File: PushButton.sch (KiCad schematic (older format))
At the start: 0 parts

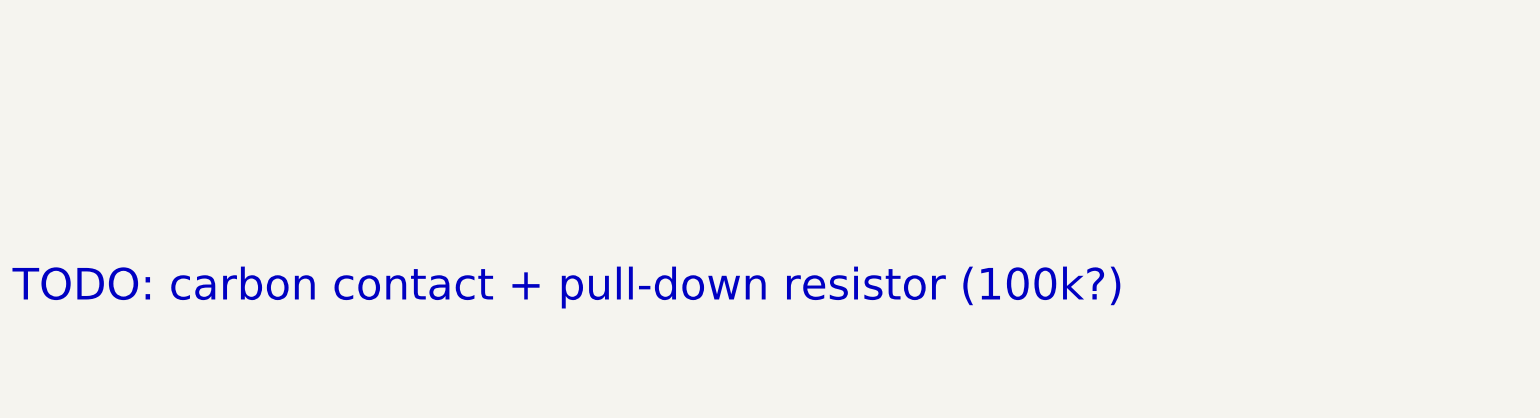
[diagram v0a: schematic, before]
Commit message: Add the push buttons and mounting holes
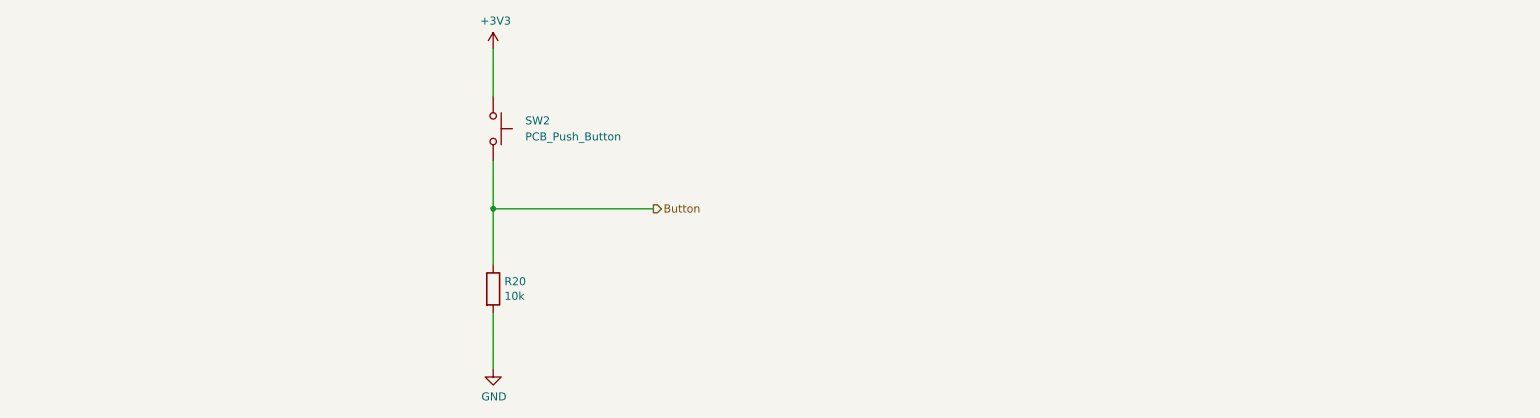
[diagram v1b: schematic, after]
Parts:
- added R19: 10k, Resistor_SMD:R_0603_1608Metric, symbol Device:R
- added SW2: PCB_Push_Button, LitterRobot:PCB_Push_Button_5mm_0.4mm, symbol Switch:SW_Push
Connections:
- new net +3V3: SW2.1
- new net Button: R19.1, SW2.2
- new net GND: R19.2
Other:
- note removed: "TODO: carbon contact + pull-down resistor (100k?)"
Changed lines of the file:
@@
 $Descr A4 11693 8268
 encoding utf-8
-Sheet 10 16
-Title "Litter Robot 3 - Push button"
+Sheet 9 16
+Title "Litter Robot 3 - Push button (single)"
 Date "2021-02-28"
 Rev "A1"
@@
 Comment4 ""
 $EndDescr
-Text Notes 2000 4100 0    197  ~ 0
-TODO: carbon contact + pull-down resistor (100k?)
+$Comp
+L Device:R R?
+U 1 1 604D6269
+P 5000 4000
+AR Path="/603F20AB/604D6269" Ref="R?"  Part="1"
+AR Path="/603F1DCE/604D6269" Ref="R?"  Part="1"
+AR Path="/603E03AA/603C05C6/604D6269" Ref="R?"  Part="1"
+AR Path="/603E03AA/603C0699/604D6269" Ref="R19"  Part="1"
+AR Path="/603E03AA/603C06CF/604D6269" Ref="R?"  Part="1"
+AR Path="/603E03AA/603C09F0/604D6269" Ref="R20"  Part="1"
+F 0 "R20" H 5070 4046 50  0000 L CNN
+F 1 "10k" H 5070 3955 50  0000 L CNN
+F 2 "Resistor_SMD:R_0603_1608Metric" V 4930 4000 50  0001 C CNN
+F 3 "~" H 5000 4000 50  0001 C CNN
+F 4 "CR0603-FX-1002ELF" H 5000 4000 50  0001 C CNN "Part_Number"
+	1    5000 4000
+	1    0    0    -1
+$EndComp
+$Comp
+L power:+3V3 #PWR?
+U 1 1 604D6568
+P 5000 2500
+AR Path="/603E03AA/603C05C6/604D6568" Ref="#PWR?"  Part="1"
+AR Path="/603E03AA/603C0699/604D6568" Ref="#PWR033"  Part="1"
+AR Path="/603E03AA/603C06CF/604D6568" Ref="#PWR?"  Part="1"
+AR Path="/603E03AA/603C09F0/604D6568" Ref="#PWR035"  Part="1"
+F 0 "#PWR035" H 5000 2350 50  0001 C CNN
+F 1 "+3V3" H 5015 2673 50  0000 C CNN
+F 2 "" H 5000 2500 50  0001 C CNN
+F 3 "" H 5000 2500 50  0001 C CNN
+	1    5000 2500
+	1    0    0    -1
+$EndComp
+$Comp
+L power:GND #PWR?
+U 1 1 604D79CA
+P 5000 4500
+AR Path="/603E03AA/603C05C6/604D79CA" Ref="#PWR?"  Part="1"
+AR Path="/603E03AA/603C0699/604D79CA" Ref="#PWR034"  Part="1"
+AR Path="/603E03AA/603C06CF/604D79CA" Ref="#PWR?"  Part="1"
+AR Path="/603E03AA/603C09F0/604D79CA" Ref="#PWR036"  Part="1"
+F 0 "#PWR036" H 5000 4250 50  0001 C CNN
+F 1 "GND" H 5005 4327 50  0000 C CNN
+F 2 "" H 5000 4500 50  0001 C CNN
+F 3 "" H 5000 4500 50  0001 C CNN
+	1    5000 4500
+	1    0    0    -1
+$EndComp
+Wire Wire Line
+	5000 2500 5000 2800
+Wire Wire Line
+	5000 3200 5000 3500
+Wire Wire Line
+	5000 4150 5000 4500
+Wire Wire Line
+	6000 3500 5000 3500
+Connection ~ 5000 3500
+Wire Wire Line
+	5000 3500 5000 3850
+Text HLabel 6000 3500 2    50   Output ~ 0
+Button
+$Comp
+L Switch:SW_Push SW2
+U 1 1 604CFE33
+P 5000 3000
+AR Path="/603E03AA/603C09F0/604CFE33" Ref="SW2"  Part="1"
+AR Path="/603E03AA/603C05C6/604CFE33" Ref="SW?"  Part="1"
+AR Path="/603E03AA/603C0699/604CFE33" Ref="SW1"  Part="1"
+AR Path="/603E03AA/603C06CF/604CFE33" Ref="SW?"  Part="1"
+F 0 "SW2" V 4950 3200 50  0000 L CNN
+F 1 "PCB_Push_Button" V 5050 3200 50  0000 L CNN
+F 2 "LitterRobot:PCB_Push_Button_5mm_0.4mm" H 5000 3200 50  0001 C CNN
+F 3 "~" H 5000 3200 50  0001 C CNN
+	1    5000 3000
+	0    1    1    0
+$EndComp
 $EndSCHEMATC
